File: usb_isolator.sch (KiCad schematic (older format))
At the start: 32 parts, among them J1 USB_1, J2 JACK_2P, J3 USB_1, SW2 SW_PUSH, U1 ADUM4160, U2 7805

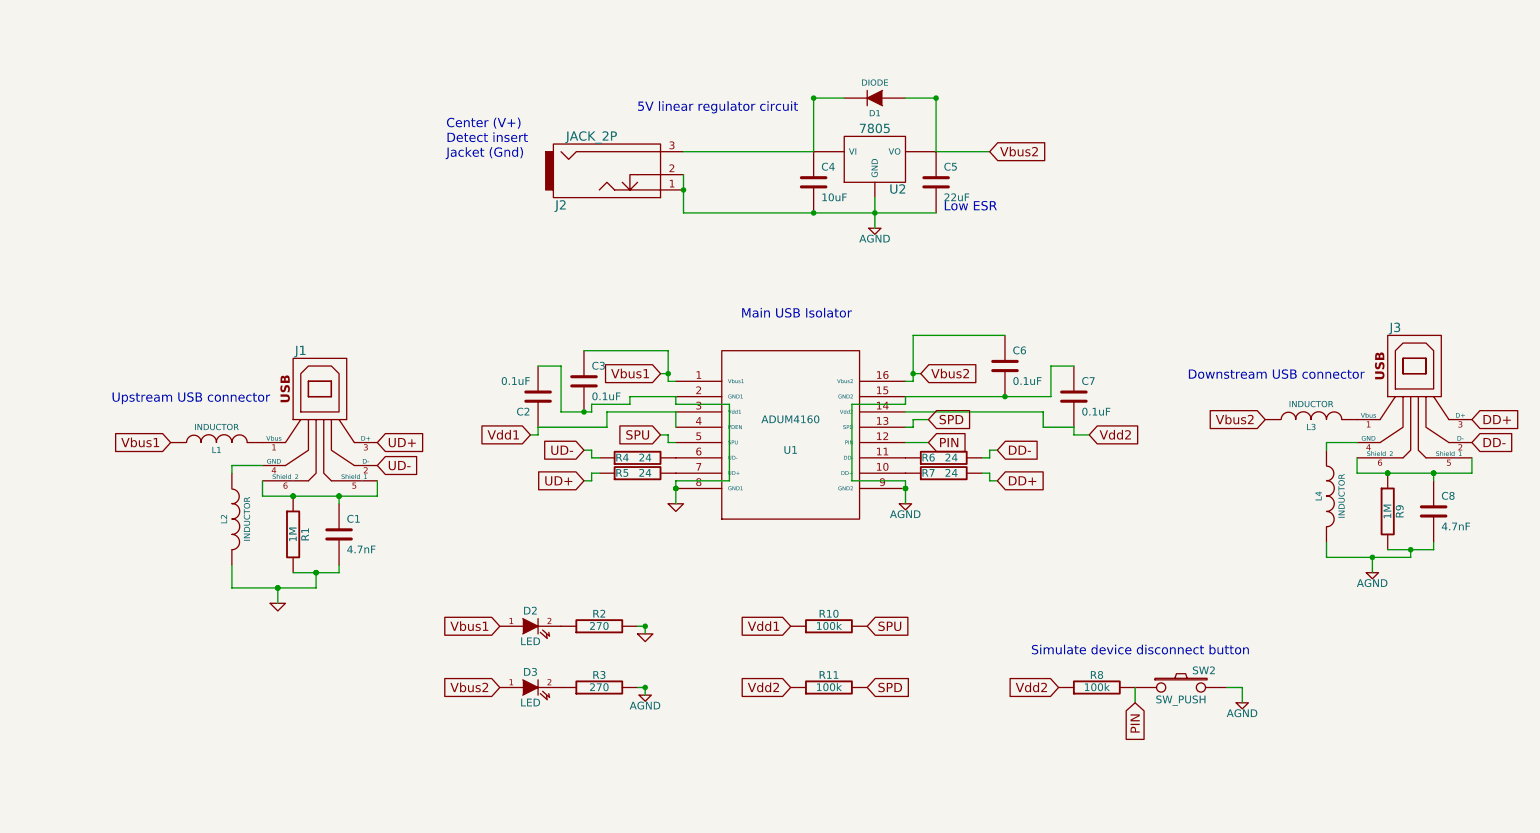
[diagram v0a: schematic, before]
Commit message: Shrunk smd footprints to 0603
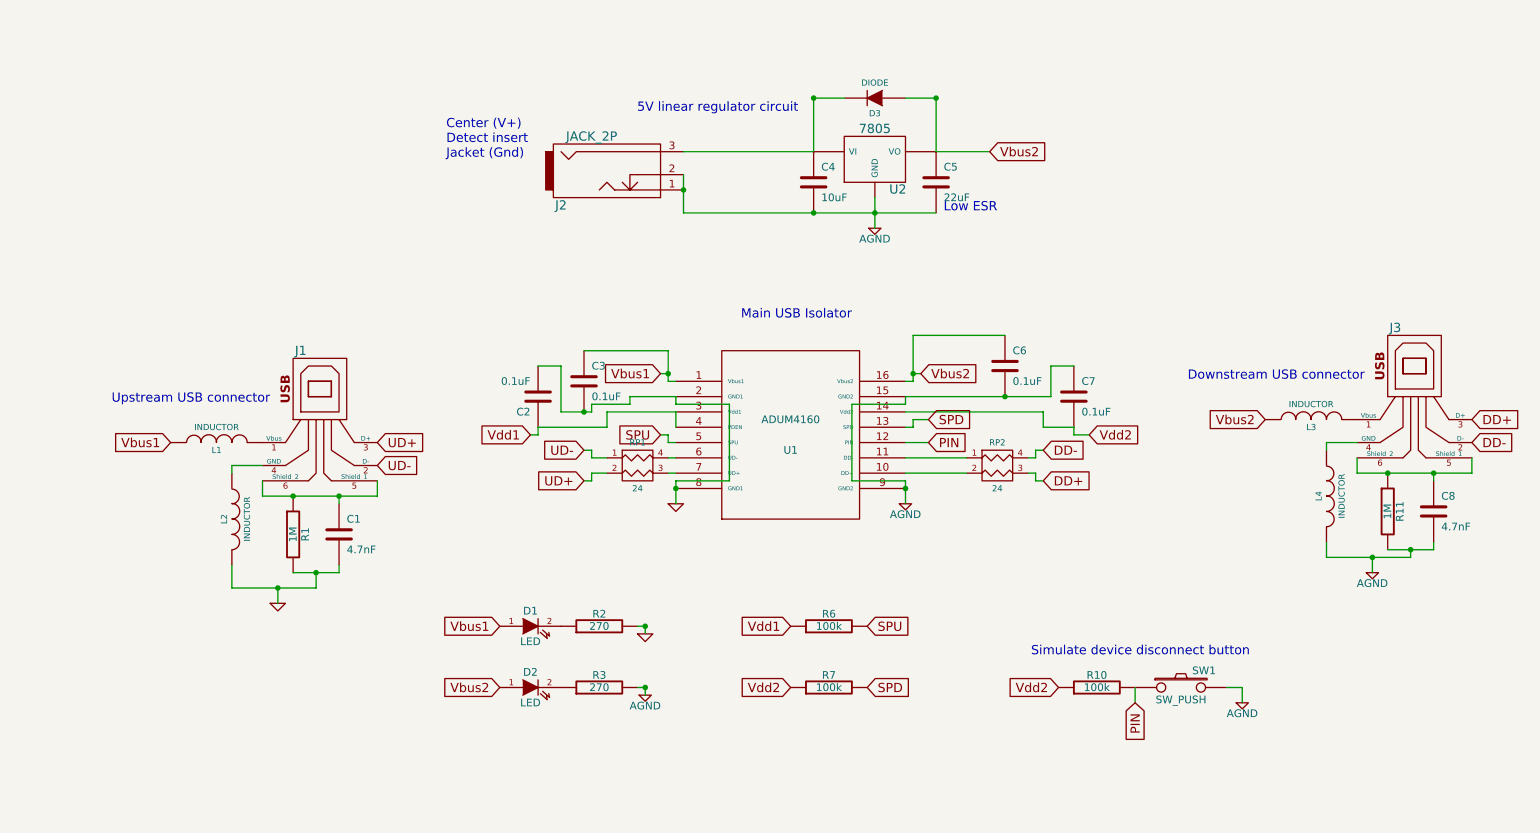
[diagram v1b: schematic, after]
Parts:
- removed R4, R5, R6, R7: 24, symbol R
- added RP1, RP2: 24, symbol R_PACK2
- renumbered D2 to D1, D3 to D2, D1 to D3, R8 to R10, R9 to R11, R10 to R6, R11 to R7, SW2 to SW1
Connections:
- net DD+: now also RP2.3 (R2)
- net DD-: now also RP2.4 (R1)
- net UD+: now also RP1.2 (P2)
- net UD-: now also RP1.1 (P1)
- net at U1.10 (DD+): now also RP2.2 (P2)
- net at U1.11 (DD-): now also RP2.1 (P1)
- net at U1.6 (UD-): now also RP1.4 (R1)
- net at U1.7 (UD+): now also RP1.3 (R2)

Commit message: Added microusb on upstream
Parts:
- added U3, U4: MICRO-B_USB, symbol MICRO-B_USB
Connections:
- net UD+: now also U3.3 (D+)
- net UD-: now also U3.2 (D-)
- net at J1.1 (Vbus), L1.2: now also U3.1 (VBUS)
- net at J1.4 (GND), L2.1: now also U3.5 (GND)
- no-connect marks 0 -> 1
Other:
- note added: "Upstream USB-B connector"
- note added: "Upstream micro-USB-B connector"
- note removed: "Upstream USB connector"

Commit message: Added microusb for device power
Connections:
- net AGND: now also U4.5 (GND)
- net Vbus2: now also U4.1 (VBUS)
- no-connect marks 1 -> 4
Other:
- note added: "Upstream micro-USB-B\nFOR POWER ONLY"
- moved on the sheet: U4
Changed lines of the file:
@@
 L MICRO-B_USB U4
 U 1 1 52CC609F
-P 8150 1950
-F 0 "U4" H 8150 1650 50  0000 C CNN
-F 1 "MICRO-B_USB" H 8150 2250 50  0000 C CNN
-F 2 "" H 8150 1950 60  0000 C CNN
-F 3 "" H 8150 1950 60  0000 C CNN
-	1    8150 1950
+P 7800 2250
+F 0 "U4" H 7800 1950 50  0000 C CNN
+F 1 "MICRO-B_USB" H 7800 2550 50  0000 C CNN
+F 2 "" H 7800 2250 60  0000 C CNN
+F 3 "" H 7800 2250 60  0000 C CNN
+	1    7800 2250
 	1    0    0    -1
 $EndComp
@@
 Wire Wire Line
 	6450 2300 6800 2300
-Wire Wire Line
-	5650 2300 4800 2300
 Connection ~ 4800 2550
 Connection ~ 5650 2700
@@
 Wire Wire Line
 	1750 4400 1850 4400
+Wire Wire Line
+	5650 2300 4800 2300
+Text Notes 8350 1800 2    60   ~ 0
+Upstream micro-USB-B\nFOR POWER ONLY
+Wire Wire Line
+	6450 2700 6450 2750
+Wire Wire Line
+	6450 2750 8000 2750
+Wire Wire Line
+	8000 2750 8000 2450
+Wire Wire Line
+	8000 2050 8100 2050
+Wire Wire Line
+	8100 2050 8100 1900
+Wire Wire Line
+	8100 1900 6650 1900
+Wire Wire Line
+	6650 1900 6650 2300
+Connection ~ 6650 2300
+NoConn ~ 8000 2150
+NoConn ~ 8000 2250
+NoConn ~ 8000 2350
 $EndSCHEMATC

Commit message: Changed regulator capacitor values
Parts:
- C4: value 10uF -> 100nF
- C5: value 22uF -> 10uF
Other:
- note removed: "Low ESR"
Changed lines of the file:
@@
 P 5650 2500
 F 0 "C4" H 5700 2600 50  0000 L CNN
-F 1 "10uF" H 5700 2400 50  0000 L CNN
+F 1 "100nF" H 5700 2400 50  0000 L CNN
 F 2 "" H 5650 2500 60  0001 C CNN
 F 3 "" H 5650 2500 60  0001 C CNN
@@
 P 6450 2500
 F 0 "C5" H 6500 2600 50  0000 L CNN
-F 1 "22uF" H 6500 2400 50  0000 L CNN
+F 1 "10uF" H 6500 2400 50  0000 L CNN
 F 2 "" H 6450 2500 60  0001 C CNN
 F 3 "" H 6450 2500 60  0001 C CNN
@@
 Text GLabel 6800 2300 2    60   Input ~ 0
 Vbus2
-Text Notes 6850 2700 2    60   ~ 0
-Low ESR
 Text Notes 8500 5600 2    60   ~ 0
 Simulate device disconnect button

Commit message: Reg bypass jumper, moved LED, enlarged board
Small changes from rev2. Board enlarged 0.25mm in all directions, LED moved away from usb-b conn, and a jumper added to bypass the regulator.
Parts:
- added JP1: JUMPER, symbol JUMPER
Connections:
- net Vbus2: now also JP1.2
- net at C4.1, D3.2 (K), J2.3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: now also JP1.1
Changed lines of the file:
@@
 $EndComp
 $Comp
-L GND #PWR01
+L GND #PWR1
 U 1 1 4F95AA45
 P 2150 5250
-F 0 "#PWR01" H 2150 5250 30  0001 C CNN
+F 0 "#PWR1" H 2150 5250 30  0001 C CNN
 F 1 "GND" H 2150 5180 30  0001 C CNN
 F 2 "" H 2150 5250 60  0001 C CNN
@@
 $EndComp
 $Comp
-L AGND #PWR02
+L AGND #PWR8
 U 1 1 4F95AD8E
 P 9300 5050
-F 0 "#PWR02" H 9300 5050 40  0001 C CNN
+F 0 "#PWR8" H 9300 5050 40  0001 C CNN
 F 1 "AGND" H 9300 4980 50  0000 C CNN
 F 2 "" H 9300 5050 60  0001 C CNN
@@
 Vdd2
 $Comp
-L AGND #PWR03
+L AGND #PWR7
 U 1 1 4F95D491
 P 8450 5900
-F 0 "#PWR03" H 8450 5900 40  0001 C CNN
+F 0 "#PWR7" H 8450 5900 40  0001 C CNN
 F 1 "AGND" H 8450 5830 50  0000 C CNN
 F 2 "" H 8450 5900 60  0001 C CNN
@@
 $EndComp
 $Comp
-L AGND #PWR04
+L AGND #PWR5
 U 1 1 4F95D7E1
 P 6050 2800
-F 0 "#PWR04" H 6050 2800 40  0001 C CNN
+F 0 "#PWR5" H 6050 2800 40  0001 C CNN
 F 1 "AGND" H 6050 2730 50  0000 C CNN
 F 2 "" H 6050 2800 60  0001 C CNN
@@
 $EndComp
 $Comp
-L GND #PWR05
+L GND #PWR4
 U 1 1 4F96DC0B
 P 4750 4600
-F 0 "#PWR05" H 4750 4600 30  0001 C CNN
+F 0 "#PWR4" H 4750 4600 30  0001 C CNN
 F 1 "GND" H 4750 4530 30  0001 C CNN
 F 2 "" H 4750 4600 60  0001 C CNN
@@
 $EndComp
 $Comp
-L AGND #PWR06
+L AGND #PWR6
 U 1 1 4F96DD11
 P 6250 4600
-F 0 "#PWR06" H 6250 4600 40  0001 C CNN
+F 0 "#PWR6" H 6250 4600 40  0001 C CNN
 F 1 "AGND" H 6250 4530 50  0000 C CNN
 F 2 "" H 6250 4600 60  0001 C CNN
@@
 $EndComp
 $Comp
-L AGND #PWR07
+L AGND #PWR3
 U 1 1 4F98924F
 P 4550 5850
-F 0 "#PWR07" H 4550 5850 40  0001 C CNN
+F 0 "#PWR3" H 4550 5850 40  0001 C CNN
 F 1 "AGND" H 4550 5780 50  0000 C CNN
 F 2 "" H 4550 5850 60  0001 C CNN
@@
 $EndComp
 $Comp
-L GND #PWR08
+L GND #PWR2
 U 1 1 4F98925E
 P 4550 5450
-F 0 "#PWR08" H 4550 5450 30  0001 C CNN
+F 0 "#PWR2" H 4550 5450 30  0001 C CNN
 F 1 "GND" H 4550 5380 30  0001 C CNN
 F 2 "" H 4550 5450 60  0001 C CNN
@@
 	4550 5400 4550 5450
 Wire Wire Line
-	5650 1950 5650 2300
-Wire Wire Line
-	6450 1950 6450 2300
+	5650 1600 5650 2300
+Wire Wire Line
+	6450 1600 6450 2300
 Connection ~ 6250 4500
 Connection ~ 4750 4500
@@
 NoConn ~ 8000 2250
 NoConn ~ 8000 2350
+$Comp
+L JUMPER JP1
+U 1 1 5363D12F
+P 6050 1600
+F 0 "JP1" H 6050 1750 60  0000 C CNN
+F 1 "JUMPER" H 6050 1520 40  0000 C CNN
+F 2 "" H 6050 1600 60  0000 C CNN
+F 3 "" H 6050 1600 60  0000 C CNN
+	1    6050 1600
+	1    0    0    -1
+$EndComp
+Wire Wire Line
+	6450 1600 6350 1600
+Wire Wire Line
+	5650 1600 5750 1600
 $EndSCHEMATC
